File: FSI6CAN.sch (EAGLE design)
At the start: 32 parts, among them IC1 ATMEGA32M1, U1 MCP2551

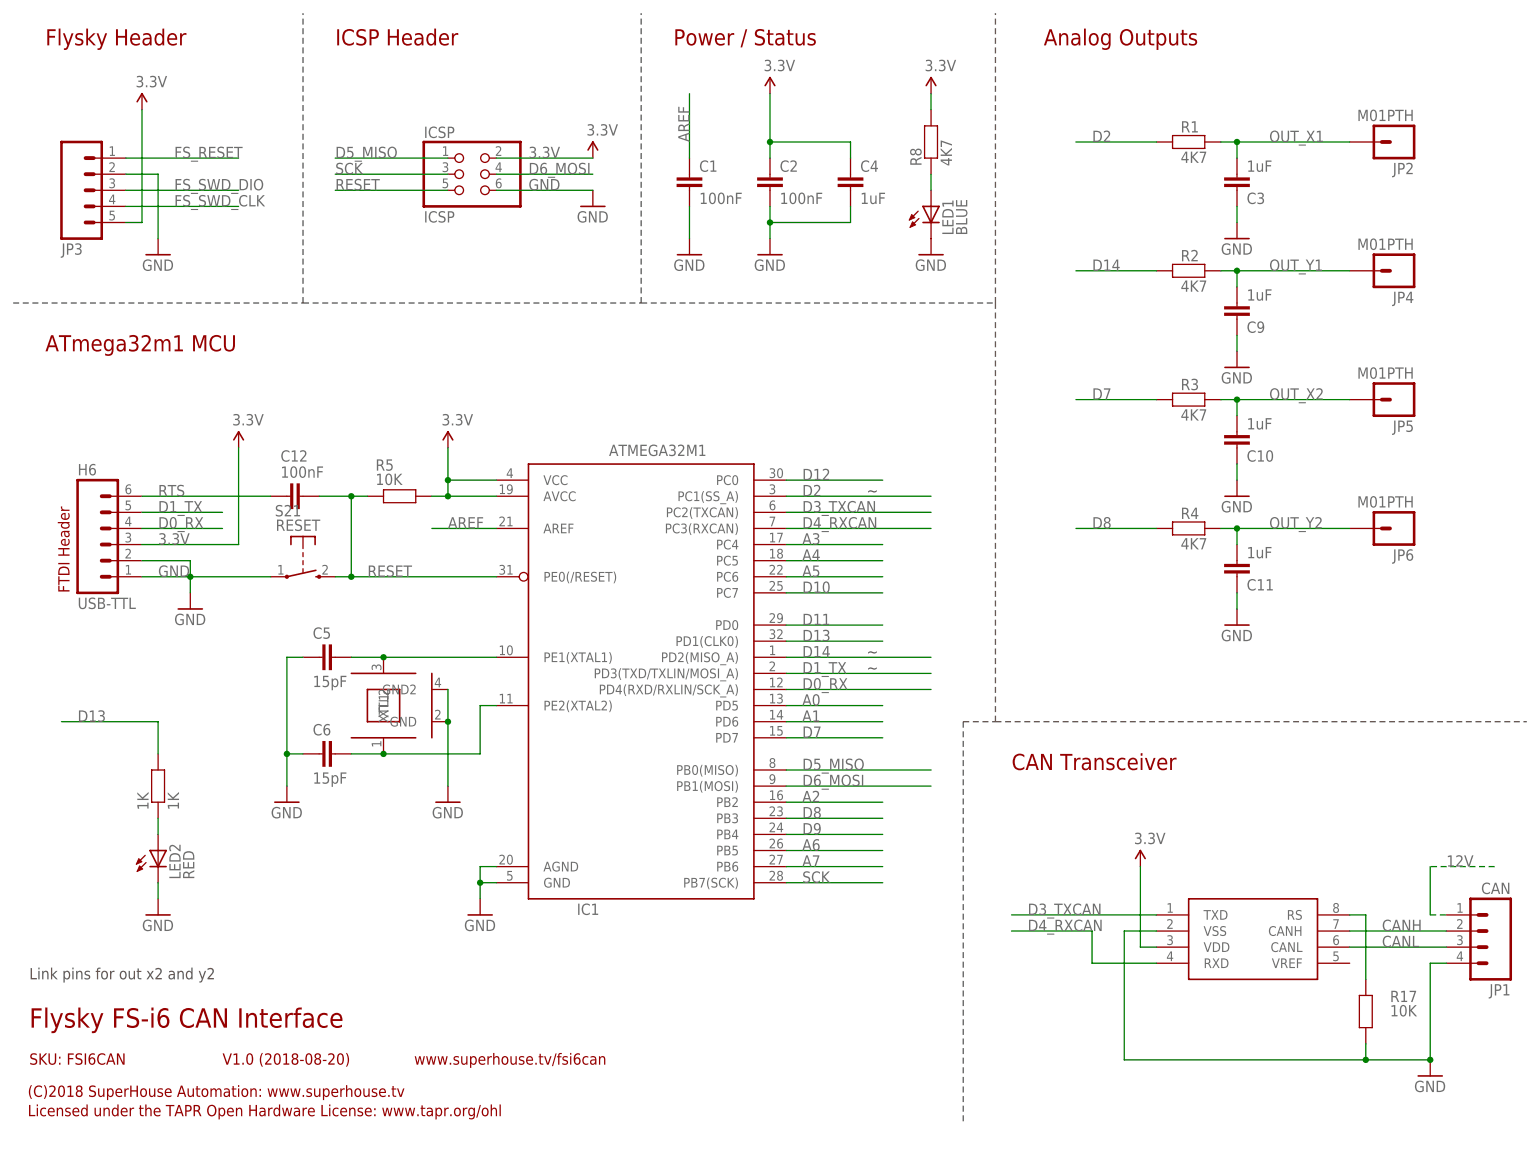
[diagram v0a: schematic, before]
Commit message: Improved designators
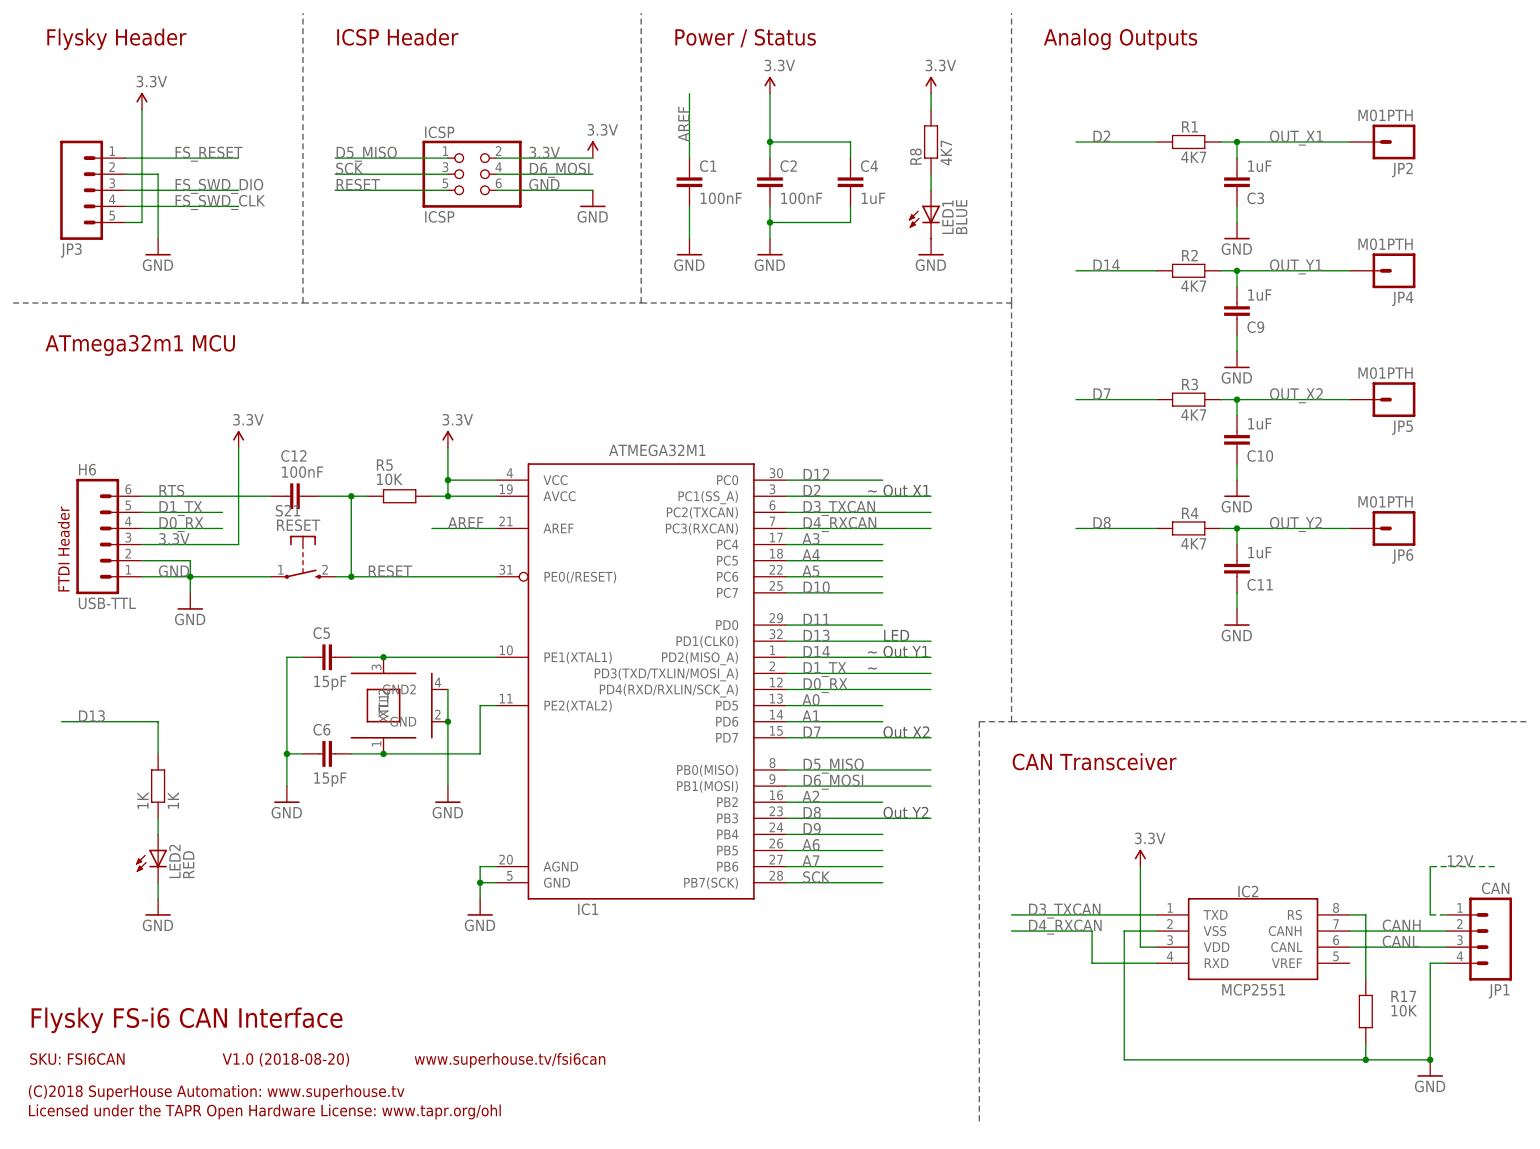
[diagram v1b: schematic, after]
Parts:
- renumbered U1 to IC2
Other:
- note added: "LED"
- note added: "Out X1"
- note added: "Out X2"
- note added: "Out Y1"
- note added: "Out Y2"
- note removed: "Link pins for out x2 and y2"
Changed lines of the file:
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@@
 <part name="C1" library="freetronics-master-v1.1" deviceset="CAP" device="0603" value="100nF"/>
 <part name="GND11" library="SparkFun" deviceset="GND" device=""/>
-<part name="ICSP" library="pinhead" deviceset="PINHD-2X3" device="" value="ICSP"/>
-<part name="GND9" library="supply1" deviceset="GND" device=""/>
+<part name="ICSP" library="pinhead" library_urn="urn:adsk.eagle:library:325" deviceset="PINHD-2X3" device="" package3d_urn="urn:adsk.eagle:package:22462/2" value="ICSP"/>
+<part name="GND9" library="supply1" library_urn="urn:adsk.eagle:library:371" deviceset="GND" device=""/>
 <part name="S21" library="freetronics-jon" deviceset="TAC_SWITCH_2PIN" device="SMT" value="RESET"/>
 <part name="GND15" library="SparkFun" deviceset="GND" device=""/>
@@
 <part name="R8" library="freetronics-jon" deviceset="RESISTOR" device="0603" value="4K7"/>
 <part name="LED1" library="freetronics-jon" deviceset="LED" device="0603" value="BLUE"/>
-<part name="U1" library="freetronics-original" deviceset="MCP2551" device=""/>
+<part name="IC2" library="freetronics-original" deviceset="MCP2551" device=""/>
 <part name="R17" library="freetronics-master-v1.1" deviceset="RESISTOR" device="0603" value="10K"/>
 <part name="JP1" library="freetronics-jon" deviceset="M04" device="PTH" value="CAN"/>
@@
 <wire x1="5.08" y1="134.62" x2="50.8" y2="134.62" width="0.1524" layer="97" style="longdash"/>
 <wire x1="50.8" y1="134.62" x2="104.14" y2="134.62" width="0.1524" layer="97" style="longdash"/>
-<wire x1="104.14" y1="134.62" x2="160.02" y2="134.62" width="0.1524" layer="97" style="longdash"/>
+<wire x1="104.14" y1="134.62" x2="162.56" y2="134.62" width="0.1524" layer="97" style="longdash"/>
 <wire x1="104.14" y1="134.62" x2="104.14" y2="180.34" width="0.1524" layer="97" style="longdash"/>
 <text x="13.97" y="88.9" size="1.778" layer="94" rot="R90">FTDI Header</text>
@@
 <wire x1="50.8" y1="134.62" x2="50.8" y2="180.34" width="0.1524" layer="97" style="longdash"/>
 <text x="55.88" y="175.26" size="2.54" layer="94" ratio="12">ICSP Header</text>
-<wire x1="154.94" y1="68.58" x2="160.02" y2="68.58" width="0.1524" layer="97" style="longdash"/>
-<wire x1="160.02" y1="68.58" x2="243.84" y2="68.58" width="0.1524" layer="97" style="longdash"/>
-<wire x1="154.94" y1="68.58" x2="154.94" y2="5.08" width="0.1524" layer="97" style="longdash"/>
-<wire x1="160.02" y1="134.62" x2="160.02" y2="180.34" width="0.1524" layer="97" style="longdash"/>
-<text x="7.62" y="27.94" size="1.778" layer="97">Link pins for out x2 and y2</text>
-<wire x1="160.02" y1="68.58" x2="160.02" y2="134.62" width="0.1524" layer="97" style="longdash"/>
+<wire x1="157.48" y1="68.58" x2="162.56" y2="68.58" width="0.1524" layer="97" style="longdash"/>
+<wire x1="162.56" y1="68.58" x2="243.84" y2="68.58" width="0.1524" layer="97" style="longdash"/>
+<wire x1="157.48" y1="68.58" x2="157.48" y2="5.08" width="0.1524" layer="97" style="longdash"/>
+<wire x1="162.56" y1="134.62" x2="162.56" y2="180.34" width="0.1524" layer="97" style="longdash"/>
+<wire x1="162.56" y1="68.58" x2="162.56" y2="134.62" width="0.1524" layer="97" style="longdash"/>
+<text x="142.24" y="53.34" size="1.778" layer="97">Out Y2</text>
+<text x="142.24" y="66.04" size="1.778" layer="97">Out X2</text>
+<text x="142.24" y="104.14" size="1.778" layer="97">Out X1</text>
+<text x="142.24" y="78.74" size="1.778" layer="97">Out Y1</text>
+<text x="142.24" y="81.28" size="1.778" layer="97">LED</text>
 </plain>
 <instances>
@@
 <attribute name="VALUE" x="155.575" y="145.288" size="1.778" layer="96" rot="R90"/>
 </instance>
-<instance part="U1" gate="G$1" x="195.58" y="30.48" smashed="yes"/>
+<instance part="IC2" gate="G$1" x="195.58" y="30.48" smashed="yes">
+<attribute name="NAME" x="198.12" y="40.894" size="1.778" layer="95"/>
+<attribute name="VALUE" x="195.58" y="25.4" size="1.778" layer="96"/>
+</instance>
 <instance part="R17" gate="G$1" x="218.44" y="22.86" smashed="yes" rot="R90">
 <attribute name="NAME" x="222.25" y="24.3586" size="1.778" layer="95"/>
@@
 <pinref part="R17" gate="G$1" pin="1"/>
 <wire x1="218.44" y1="15.24" x2="218.44" y2="17.78" width="0.1524" layer="91"/>
-<pinref part="U1" gate="G$1" pin="VSS"/>
+<pinref part="IC2" gate="G$1" pin="VSS"/>
 <wire x1="185.42" y1="35.56" x2="180.34" y2="35.56" width="0.1524" layer="91"/>
 <wire x1="180.34" y1="35.56" x2="180.34" y2="15.24" width="0.1524" layer="91"/>
@@
 <net name="CANH" class="0">
 <segment>
-<pinref part="U1" gate="G$1" pin="CANH"/>
+<pinref part="IC2" gate="G$1" pin="CANH"/>
 <wire x1="215.9" y1="35.56" x2="231.14" y2="35.56" width="0.1524" layer="91"/>
 <label x="220.98" y="35.56" size="1.778" layer="95"/>
@@
 <net name="CANL" class="0">
 <segment>
-<pinref part="U1" gate="G$1" pin="CANL"/>
+<pinref part="IC2" gate="G$1" pin="CANL"/>
 <wire x1="215.9" y1="33.02" x2="231.14" y2="33.02" width="0.1524" layer="91"/>
 <label x="220.98" y="33.02" size="1.778" layer="95"/>
@@
 <net name="N$16" class="0">
 <segment>
-<pinref part="U1" gate="G$1" pin="RS"/>
+<pinref part="IC2" gate="G$1" pin="RS"/>
 <wire x1="215.9" y1="38.1" x2="218.44" y2="38.1" width="0.1524" layer="91"/>
 <pinref part="R17" gate="G$1" pin="2"/>
@@
 </segment>
 <segment>
-<pinref part="U1" gate="G$1" pin="VDD"/>
+<pinref part="IC2" gate="G$1" pin="VDD"/>
 <wire x1="185.42" y1="33.02" x2="182.88" y2="33.02" width="0.1524" layer="91"/>
 <wire x1="182.88" y1="33.02" x2="182.88" y2="45.72" width="0.1524" layer="91"/>
@@
 </segment>
 <segment>
-<pinref part="U1" gate="G$1" pin="TXD"/>
+<pinref part="IC2" gate="G$1" pin="TXD"/>
 <wire x1="162.56" y1="38.1" x2="185.42" y2="38.1" width="0.1524" layer="91"/>
 <label x="165.1" y="38.1" size="1.778" layer="95"/>
@@
 </segment>
 <segment>
-<pinref part="U1" gate="G$1" pin="RXD"/>
+<pinref part="IC2" gate="G$1" pin="RXD"/>
 <wire x1="185.42" y1="30.48" x2="175.26" y2="30.48" width="0.1524" layer="91"/>
 <wire x1="175.26" y1="30.48" x2="175.26" y2="35.56" width="0.1524" layer="91"/>
@@
 <segment>
 <pinref part="IC1" gate="G$1" pin="PD7"/>
-<wire x1="127" y1="66.04" x2="142.24" y2="66.04" width="0.1524" layer="91"/>
+<wire x1="127" y1="66.04" x2="149.86" y2="66.04" width="0.1524" layer="91"/>
 <label x="129.54" y="66.04" size="1.778" layer="95"/>
 </segment>
@@
 <segment>
 <pinref part="IC1" gate="G$1" pin="PD1(CLK0)"/>
-<wire x1="127" y1="81.28" x2="142.24" y2="81.28" width="0.1524" layer="91"/>
+<wire x1="127" y1="81.28" x2="149.86" y2="81.28" width="0.1524" layer="91"/>
 <label x="129.54" y="81.28" size="1.778" layer="95"/>
 </segment>
@@
 <segment>
 <pinref part="IC1" gate="G$1" pin="PB3"/>
-<wire x1="127" y1="53.34" x2="142.24" y2="53.34" width="0.1524" layer="91"/>
+<wire x1="127" y1="53.34" x2="149.86" y2="53.34" width="0.1524" layer="91"/>
 <label x="129.54" y="53.34" size="1.778" layer="95"/>
 </segment>
@@
 </schematic>
 </drawing>
+<compatibility>
+<note version="8.2" severity="warning">
+Since Version 8.2, EAGLE supports online libraries. The ids
+of those online libraries will not be understood (or retained)
+with this version.
+</note>
+<note version="8.3" severity="warning">
+Since Version 8.3, EAGLE supports URNs for individual library
+assets (packages, symbols, and devices). The URNs of those assets
+will not be understood (or retained) with this version.
+</note>
+<note version="8.3" severity="warning">
+Since Version 8.3, EAGLE supports the association of 3D packages
+with devices in libraries, schematics, and board files. Those 3D
+packages will not be understood (or retained) with this version.
+</note>
+</compatibility>
 </eagle>

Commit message: Changed I/O pin for output Y2 and switch ICSP to other SPI port
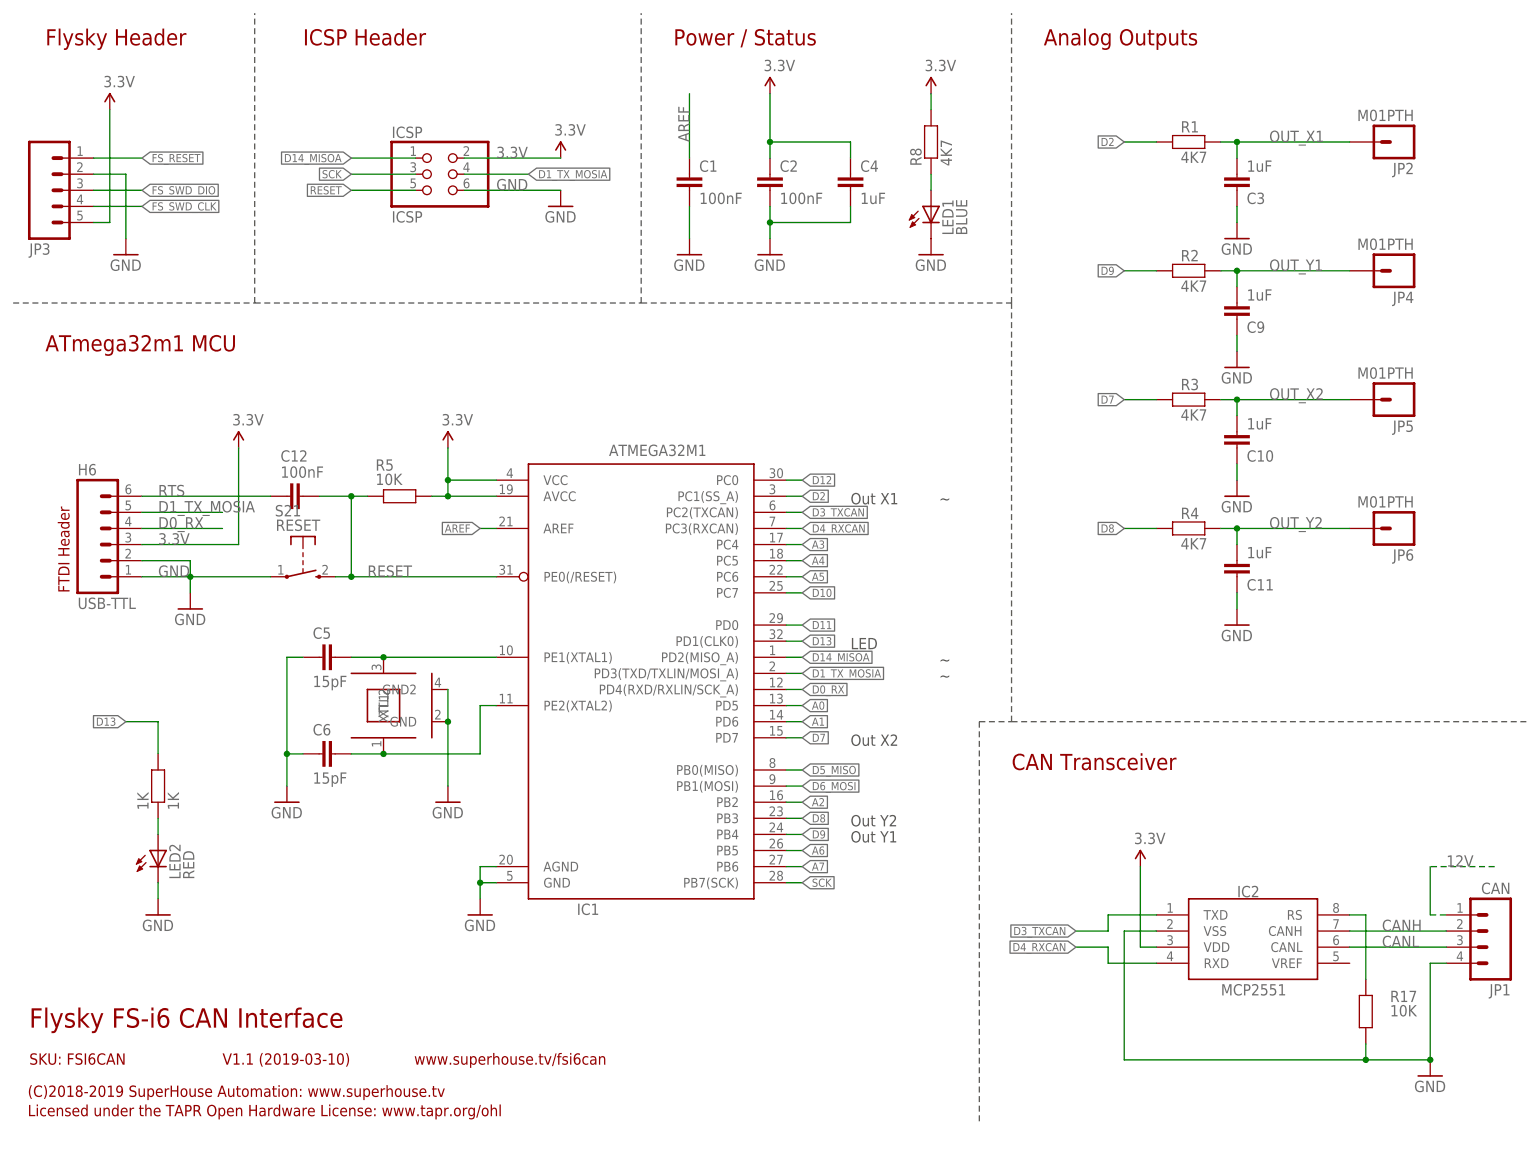
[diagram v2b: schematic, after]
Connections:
- removed net D14: IC1.PD2(MISO_A), R2.1
- removed net D1_TX: H6.5, IC1.PD3(TXD/TXLIN/MOSI_A)
- new net D14_MISOA: IC1.PD2(MISO_A), ICSP.1
- new net D1_TX_MOSIA: H6.5, IC1.PD3(TXD/TXLIN/MOSI_A), ICSP.4
- net D5_MISO: no longer ICSP.1
- net D6_MOSI: no longer ICSP.4
- net D9: now also R2.1
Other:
- note added: "(C)2018-2019 SuperHouse Automation: www.superhouse.tv"
- note added: "V1.1 (2019-03-10)"
- note removed: "(C)2018 SuperHouse Automation: www.superhouse.tv"
- note removed: "V1.0 (2018-08-20)"
- moved on the sheet: ICSP, JP3
